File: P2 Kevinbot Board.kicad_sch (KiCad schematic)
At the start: 41 parts, among them J1 Screw_Terminal_01x02, J10 Conn_01x04, J11 Conn_01x04_Male, J12 Conn_02x06_Odd_Even, J13 Conn_01x04, J14 Conn_01x02, J15 Conn_01x04, J16 Conn_02x06_Odd_Even, J2 Conn_01x03_Male, J3 Screw_Terminal_01x02, J30 Conn_01x02_Pin, J31 Conn_01x02, J4 Screw_Terminal_01x02, J5 Screw_Terminal_01x02, J6 Conn_02x06_Odd_Even, J7 Conn_01x04, J8 Conn_02x06_Odd_Even, J9 Screw_Terminal_01x02, Q1 IRLML6402, SW1 SW_Push, U1 P2_EDGE_MODULE_SOCKET, U2 DS18B20

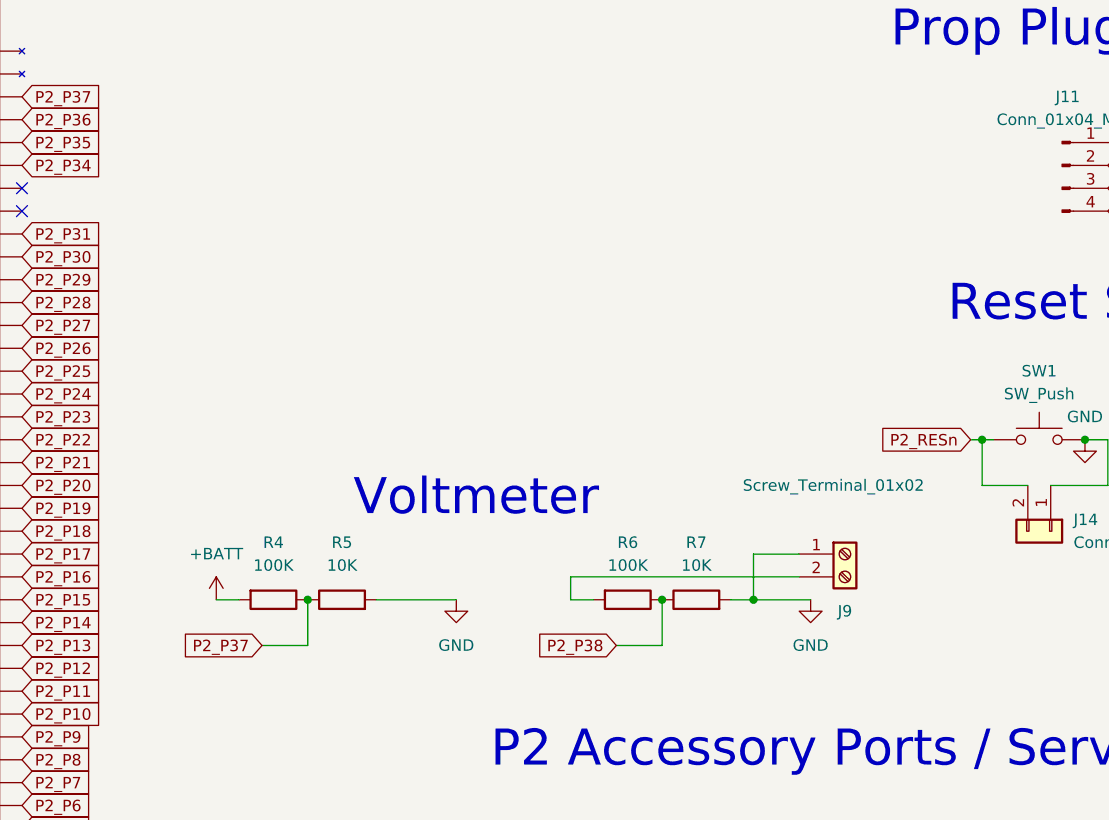
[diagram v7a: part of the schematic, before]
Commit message: Add voltmeter polyfuses
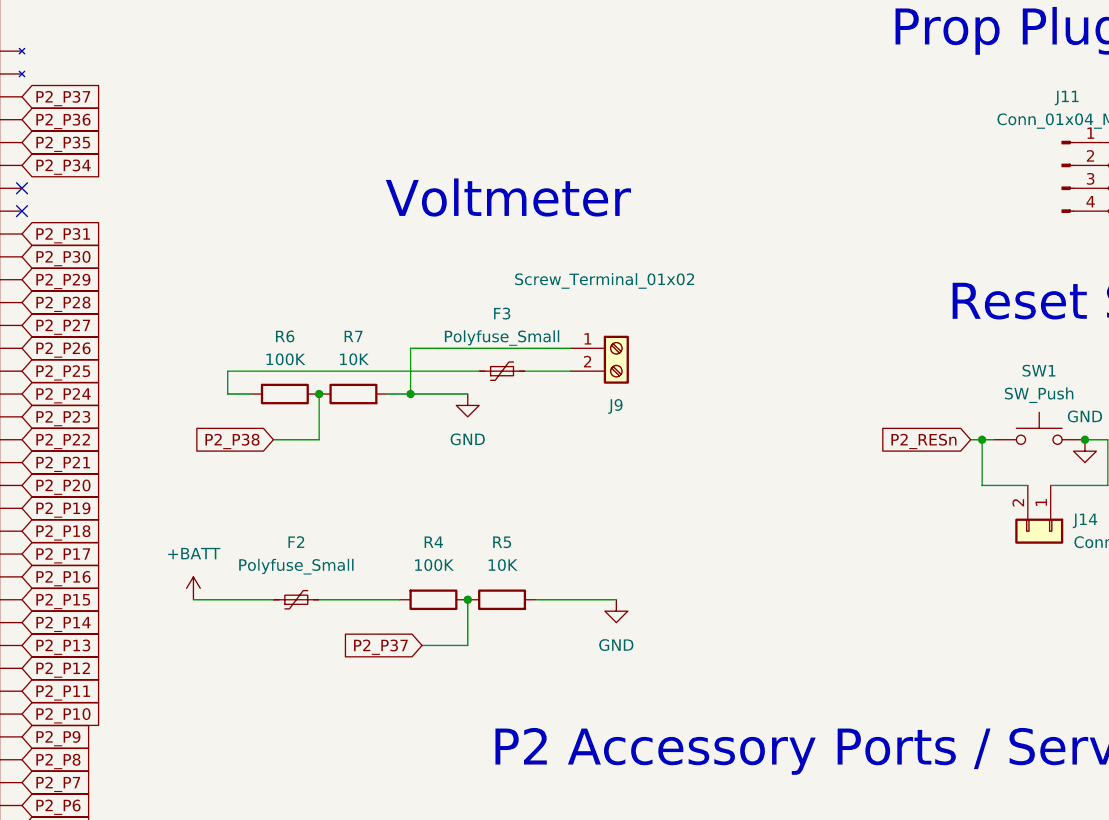
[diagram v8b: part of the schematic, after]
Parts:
- added F2, F3: Polyfuse_Small, Fuse:Fuse_1206_3216Metric_Pad1.42x1.75mm_HandSolder, symbol Device:Polyfuse_Small
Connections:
- net +BATT: now also F2.1; no longer R4.2
- net at J9.2 (Pin_2): now also F3.2; no longer R6.2
- new net: F2.2, R4.2
- new net: F3.1, R6.2
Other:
- moved on the sheet: J9, R4, R5, R6, R7
